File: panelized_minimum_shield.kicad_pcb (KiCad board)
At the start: 2 copper layers, 100 x 78 mm, 91 parts, among them J1 Conn_02x08_Odd_Even, J2 Conn_02x08_Odd_Even, J3 Conn_01x06, SW1 SW_Push

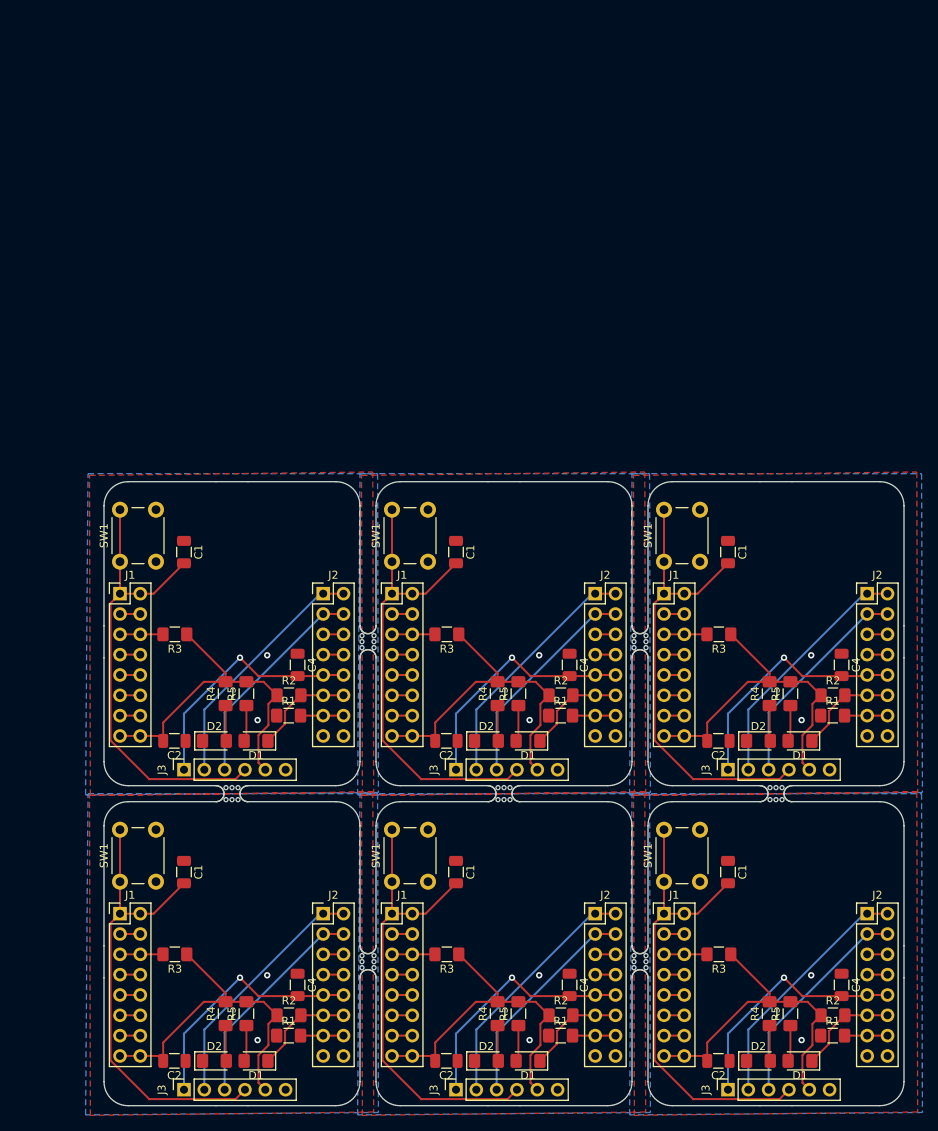
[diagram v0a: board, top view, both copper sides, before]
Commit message: V1.1 - fixing missing ground connection to pull up resistor for GPIO15
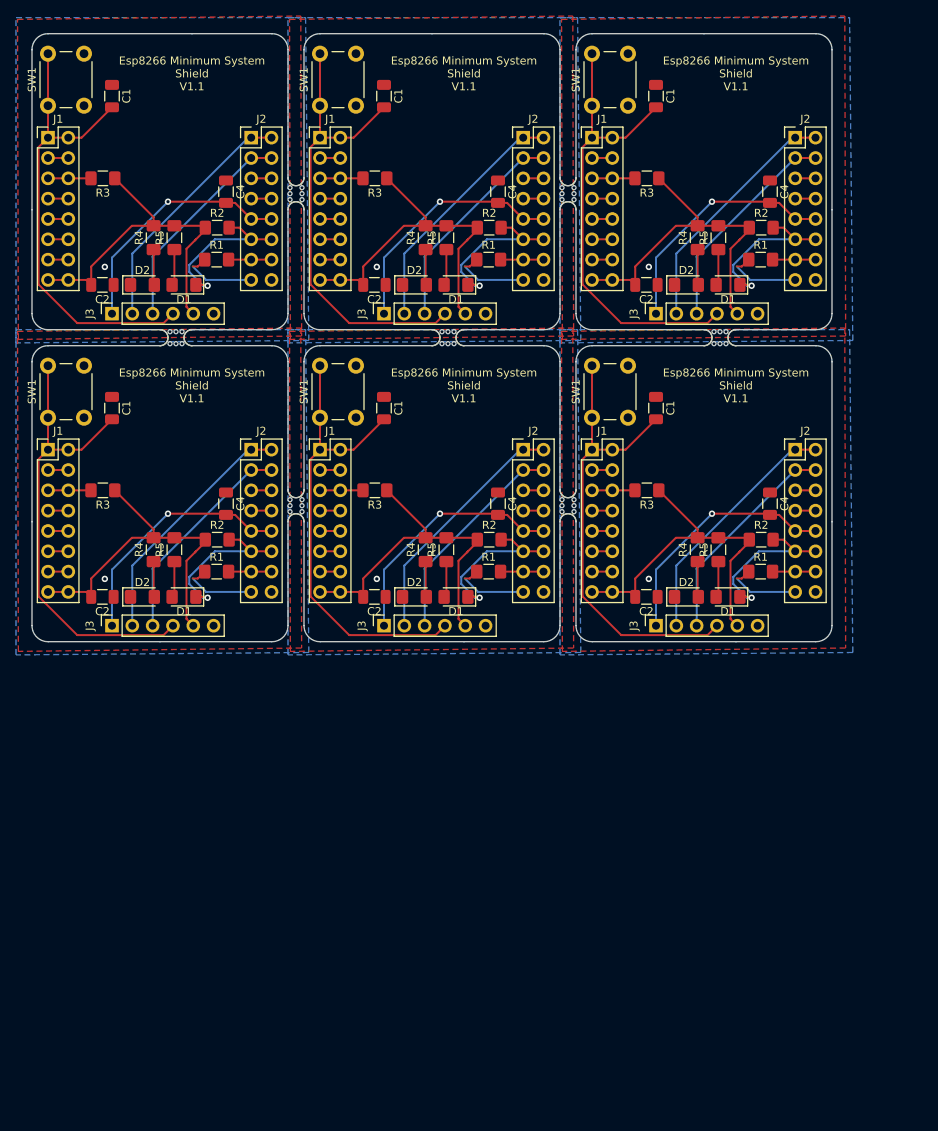
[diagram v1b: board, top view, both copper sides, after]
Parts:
- removed the C1 at (109.0, 128.8)
- removed the C1 at (75.0, 128.8)
- removed the C1 at (41.0, 128.8)
- removed the C1 at (109.0, 88.8)
- removed the C1 at (75.0, 88.8)
- removed the C2 at (107.8, 152.4)
- removed the C2 at (73.8, 152.4)
- removed the C2 at (39.8, 152.4)
- removed the C2 at (107.8, 112.4)
- removed the C2 at (73.8, 112.4)
- removed the C4 at (123.2, 142.9)
- removed the C4 at (89.2, 142.9)
- removed the C4 at (55.2, 142.9)
- removed the C4 at (123.2, 102.9)
- removed the C4 at (89.2, 102.9)
- removed the D1 at (118.0, 152.4)
- removed the D1 at (84.0, 152.4)
- removed the D1 at (50.0, 152.4)
- removed the D1 at (118.0, 112.4)
- removed the D1 at (84.0, 112.4)
- removed the D2 at (112.8, 152.4)
- removed the D2 at (78.8, 152.4)
- removed the D2 at (44.8, 152.4)
- removed the D2 at (112.8, 112.4)
- removed the D2 at (78.8, 112.4)
- removed the J1 at (101.0, 134.0)
- removed the J1 at (67.0, 134.0)
- removed the J1 at (33.0, 134.0)
- removed the J1 at (101.0, 94.0)
- removed the J1 at (67.0, 94.0)
- removed the J2 at (126.4, 134.0)
- removed the J2 at (92.4, 134.0)
- removed the J2 at (58.4, 134.0)
- removed the J2 at (126.4, 94.0)
- removed the J2 at (92.4, 94.0)
- removed the J3 at (109.0, 156.0)
- removed the J3 at (75.0, 156.0)
- removed the J3 at (41.0, 156.0)
- removed the J3 at (109.0, 116.0)
- removed the J3 at (75.0, 116.0)
- removed the R1 at (122.1, 149.2)
- removed the R1 at (88.1, 149.2)
- removed the R1 at (54.1, 149.2)
- removed the R1 at (122.1, 109.2)
- removed the R1 at (88.1, 109.2)
- removed the R2 at (122.1, 146.7)
- removed the R2 at (88.1, 146.7)
- removed the R2 at (54.1, 146.7)
- removed the R2 at (122.1, 106.7)
- removed the R2 at (88.1, 106.7)
- removed the R3 at (107.9, 139.1)
- removed the R3 at (73.9, 139.1)
- removed the R3 at (39.9, 139.1)
- removed the R3 at (107.9, 99.1)
- removed the R3 at (73.9, 99.1)
- removed the R4 at (114.2, 146.5)
- removed the R4 at (80.2, 146.5)
- removed the R4 at (46.2, 146.5)
- removed the R4 at (114.2, 106.5)
- removed the R4 at (80.2, 106.5)
- removed the R5 at (116.8, 146.5)
- removed the R5 at (82.8, 146.5)
- removed the R5 at (48.8, 146.5)
- removed the R5 at (116.8, 106.5)
- removed the R5 at (82.8, 106.5)
- removed the SW1 at (101.0, 130.0)
- removed the SW1 at (67.0, 130.0)
- removed the SW1 at (33.0, 130.0)
- removed the SW1 at (101.0, 90.0)
- removed the SW1 at (67.0, 90.0)
- removed the mouse-bite-2mm-slot at (98.0, 140.0)
- removed the mouse-bite-2mm-slot at (64.0, 140.0)
- removed the mouse-bite-2mm-slot at (98.0, 100.0)
- removed the mouse-bite-2mm-slot at (64.0, 100.0)
- removed the mouse-bite-2mm-slot at (115.0, 119.0)
- removed the mouse-bite-2mm-slot at (81.0, 119.0)
- removed the mouse-bite-2mm-slot at (47.0, 119.0)
- added C1: 100nf, Capacitor_SMD:C_1206_3216Metric, F.Cu at (100.0, 70.8)
- added C1: 100nf, Capacitor_SMD:C_1206_3216Metric, F.Cu at (66.0, 70.8)
- added C1: 100nf, Capacitor_SMD:C_1206_3216Metric, F.Cu at (32.0, 70.8)
- added C1: 100nf, Capacitor_SMD:C_1206_3216Metric, F.Cu at (100.0, 31.8)
- added C1: 100nf, Capacitor_SMD:C_1206_3216Metric, F.Cu at (66.0, 31.8)
- added C2: 100nf, Capacitor_SMD:C_1206_3216Metric, F.Cu at (98.8, 94.4)
- added C2: 100nf, Capacitor_SMD:C_1206_3216Metric, F.Cu at (64.8, 94.4)
- added C2: 100nf, Capacitor_SMD:C_1206_3216Metric, F.Cu at (30.8, 94.4)
- added C2: 100nf, Capacitor_SMD:C_1206_3216Metric, F.Cu at (98.8, 55.4)
- added C2: 100nf, Capacitor_SMD:C_1206_3216Metric, F.Cu at (64.8, 55.4)
- added C4: 100nf, Capacitor_SMD:C_1206_3216Metric, F.Cu at (114.2, 82.8)
- added C4: 100nf, Capacitor_SMD:C_1206_3216Metric, F.Cu at (80.2, 82.8)
- added C4: 100nf, Capacitor_SMD:C_1206_3216Metric, F.Cu at (46.2, 82.8)
- added C4: 100nf, Capacitor_SMD:C_1206_3216Metric, F.Cu at (114.2, 43.8)
- added C4: 100nf, Capacitor_SMD:C_1206_3216Metric, F.Cu at (80.2, 43.8)
- added D1: GREEN, LED_SMD:LED_1206_3216Metric_Pad1.42x1.75mm_HandSolder, F.Cu at (109.0, 94.4)
- added D1: GREEN, LED_SMD:LED_1206_3216Metric_Pad1.42x1.75mm_HandSolder, F.Cu at (75.0, 94.4)
- added D1: GREEN, LED_SMD:LED_1206_3216Metric_Pad1.42x1.75mm_HandSolder, F.Cu at (41.0, 94.4)
- added D1: GREEN, LED_SMD:LED_1206_3216Metric_Pad1.42x1.75mm_HandSolder, F.Cu at (109.0, 55.4)
- added D1: GREEN, LED_SMD:LED_1206_3216Metric_Pad1.42x1.75mm_HandSolder, F.Cu at (75.0, 55.4)
- added D2: RED, LED_SMD:LED_1206_3216Metric_Pad1.42x1.75mm_HandSolder, F.Cu at (103.8, 94.4)
- added D2: RED, LED_SMD:LED_1206_3216Metric_Pad1.42x1.75mm_HandSolder, F.Cu at (69.8, 94.4)
- added D2: RED, LED_SMD:LED_1206_3216Metric_Pad1.42x1.75mm_HandSolder, F.Cu at (35.8, 94.4)
- added D2: RED, LED_SMD:LED_1206_3216Metric_Pad1.42x1.75mm_HandSolder, F.Cu at (103.8, 55.4)
- added D2: RED, LED_SMD:LED_1206_3216Metric_Pad1.42x1.75mm_HandSolder, F.Cu at (69.8, 55.4)
- added J1: Conn_02x08_Odd_Even, Connector_PinHeader_2.54mm:PinHeader_2x08_P2.54mm_Vertical, F.Cu at (92.0, 76.0)
- added J1: Conn_02x08_Odd_Even, Connector_PinHeader_2.54mm:PinHeader_2x08_P2.54mm_Vertical, F.Cu at (58.0, 76.0)
- added J1: Conn_02x08_Odd_Even, Connector_PinHeader_2.54mm:PinHeader_2x08_P2.54mm_Vertical, F.Cu at (24.0, 76.0)
- added J1: Conn_02x08_Odd_Even, Connector_PinHeader_2.54mm:PinHeader_2x08_P2.54mm_Vertical, F.Cu at (92.0, 37.0)
- added J1: Conn_02x08_Odd_Even, Connector_PinHeader_2.54mm:PinHeader_2x08_P2.54mm_Vertical, F.Cu at (58.0, 37.0)
- added J2: Conn_02x08_Odd_Even, Connector_PinHeader_2.54mm:PinHeader_2x08_P2.54mm_Vertical, F.Cu at (117.4, 76.0)
- added J2: Conn_02x08_Odd_Even, Connector_PinHeader_2.54mm:PinHeader_2x08_P2.54mm_Vertical, F.Cu at (83.4, 76.0)
- added J2: Conn_02x08_Odd_Even, Connector_PinHeader_2.54mm:PinHeader_2x08_P2.54mm_Vertical, F.Cu at (49.4, 76.0)
- added J2: Conn_02x08_Odd_Even, Connector_PinHeader_2.54mm:PinHeader_2x08_P2.54mm_Vertical, F.Cu at (117.4, 37.0)
- added J2: Conn_02x08_Odd_Even, Connector_PinHeader_2.54mm:PinHeader_2x08_P2.54mm_Vertical, F.Cu at (83.4, 37.0)
- added J3: Conn_01x06, Connector_PinSocket_2.54mm:PinSocket_1x06_P2.54mm_Vertical, F.Cu at (100.0, 98.0)
- added J3: Conn_01x06, Connector_PinSocket_2.54mm:PinSocket_1x06_P2.54mm_Vertical, F.Cu at (66.0, 98.0)
- added J3: Conn_01x06, Connector_PinSocket_2.54mm:PinSocket_1x06_P2.54mm_Vertical, F.Cu at (32.0, 98.0)
- added J3: Conn_01x06, Connector_PinSocket_2.54mm:PinSocket_1x06_P2.54mm_Vertical, F.Cu at (100.0, 59.0)
- added J3: Conn_01x06, Connector_PinSocket_2.54mm:PinSocket_1x06_P2.54mm_Vertical, F.Cu at (66.0, 59.0)
- added R1: 10k, Resistor_SMD:R_1206_3216Metric_Pad1.42x1.75mm_HandSolder, F.Cu at (113.1, 91.2)
- added R1: 10k, Resistor_SMD:R_1206_3216Metric_Pad1.42x1.75mm_HandSolder, F.Cu at (79.1, 91.2)
- added R1: 10k, Resistor_SMD:R_1206_3216Metric_Pad1.42x1.75mm_HandSolder, F.Cu at (45.1, 91.2)
- added R1: 10k, Resistor_SMD:R_1206_3216Metric_Pad1.42x1.75mm_HandSolder, F.Cu at (113.1, 52.2)
- added R1: 10k, Resistor_SMD:R_1206_3216Metric_Pad1.42x1.75mm_HandSolder, F.Cu at (79.1, 52.2)
- added R2: 5k1, Resistor_SMD:R_1206_3216Metric_Pad1.42x1.75mm_HandSolder, F.Cu at (113.2, 87.2)
- added R2: 5k1, Resistor_SMD:R_1206_3216Metric_Pad1.42x1.75mm_HandSolder, F.Cu at (79.2, 87.2)
- added R2: 5k1, Resistor_SMD:R_1206_3216Metric_Pad1.42x1.75mm_HandSolder, F.Cu at (45.1, 87.2)
- added R2: 5k1, Resistor_SMD:R_1206_3216Metric_Pad1.42x1.75mm_HandSolder, F.Cu at (113.2, 48.2)
- added R2: 5k1, Resistor_SMD:R_1206_3216Metric_Pad1.42x1.75mm_HandSolder, F.Cu at (79.2, 48.2)
- added R3: 5k1, Resistor_SMD:R_1206_3216Metric_Pad1.42x1.75mm_HandSolder, F.Cu at (98.9, 81.1)
- added R3: 5k1, Resistor_SMD:R_1206_3216Metric_Pad1.42x1.75mm_HandSolder, F.Cu at (64.9, 81.1)
- added R3: 5k1, Resistor_SMD:R_1206_3216Metric_Pad1.42x1.75mm_HandSolder, F.Cu at (30.9, 81.1)
- added R3: 5k1, Resistor_SMD:R_1206_3216Metric_Pad1.42x1.75mm_HandSolder, F.Cu at (98.9, 42.1)
- added R3: 5k1, Resistor_SMD:R_1206_3216Metric_Pad1.42x1.75mm_HandSolder, F.Cu at (64.9, 42.1)
- added R4: 220, Resistor_SMD:R_1206_3216Metric_Pad1.42x1.75mm_HandSolder, F.Cu at (105.2, 88.5)
- added R4: 220, Resistor_SMD:R_1206_3216Metric_Pad1.42x1.75mm_HandSolder, F.Cu at (71.2, 88.5)
- added R4: 220, Resistor_SMD:R_1206_3216Metric_Pad1.42x1.75mm_HandSolder, F.Cu at (37.2, 88.5)
- added R4: 220, Resistor_SMD:R_1206_3216Metric_Pad1.42x1.75mm_HandSolder, F.Cu at (105.2, 49.5)
- added R4: 220, Resistor_SMD:R_1206_3216Metric_Pad1.42x1.75mm_HandSolder, F.Cu at (71.2, 49.5)
- added R5: 220, Resistor_SMD:R_1206_3216Metric_Pad1.42x1.75mm_HandSolder, F.Cu at (107.8, 88.5)
- added R5: 220, Resistor_SMD:R_1206_3216Metric_Pad1.42x1.75mm_HandSolder, F.Cu at (73.8, 88.5)
- added R5: 220, Resistor_SMD:R_1206_3216Metric_Pad1.42x1.75mm_HandSolder, F.Cu at (39.8, 88.5)
- added R5: 220, Resistor_SMD:R_1206_3216Metric_Pad1.42x1.75mm_HandSolder, F.Cu at (107.8, 49.5)
- added R5: 220, Resistor_SMD:R_1206_3216Metric_Pad1.42x1.75mm_HandSolder, F.Cu at (73.8, 49.5)
- added SW1: SW_Push, Button_Switch_THT:SW_PUSH_6mm, F.Cu at (92.0, 72.0)
- added SW1: SW_Push, Button_Switch_THT:SW_PUSH_6mm, F.Cu at (58.0, 72.0)
- added SW1: SW_Push, Button_Switch_THT:SW_PUSH_6mm, F.Cu at (24.0, 72.0)
- added SW1: SW_Push, Button_Switch_THT:SW_PUSH_6mm, F.Cu at (92.0, 33.0)
- added SW1: SW_Push, Button_Switch_THT:SW_PUSH_6mm, F.Cu at (58.0, 33.0)
- added mouse-bite-2mm-slot: VAL**, Panelization:mouse-bite-2mm-slot, F.Cu at (89.0, 83.0)
- added mouse-bite-2mm-slot: VAL**, Panelization:mouse-bite-2mm-slot, F.Cu at (55.0, 83.0)
- added mouse-bite-2mm-slot: VAL**, Panelization:mouse-bite-2mm-slot, F.Cu at (89.0, 44.0)
- added mouse-bite-2mm-slot: VAL**, Panelization:mouse-bite-2mm-slot, F.Cu at (55.0, 44.0)
- added mouse-bite-2mm-slot: VAL**, Panelization:mouse-bite-2mm-slot, F.Cu at (108.0, 62.0)
- added mouse-bite-2mm-slot: VAL**, Panelization:mouse-bite-2mm-slot, F.Cu at (74.0, 62.0)
- added mouse-bite-2mm-slot: VAL**, Panelization:mouse-bite-2mm-slot, F.Cu at (40.0, 62.0)
- moved C4 59.8 mm to (46.2, 43.8)
- moved R2 59.1 mm to (45.1, 48.2)
- moved C2 57.7 mm to (30.8, 55.4)
- moved D1 57.7 mm to (41.0, 55.4)
- moved D2 57.7 mm to (35.8, 55.4)
- moved C1 57.7 mm to (32.0, 31.8)
- moved J1 57.7 mm to (24.0, 37.0)
- moved J2 57.7 mm to (49.4, 37.0)
- moved J3 57.7 mm to (32.0, 59.0)
- moved R3 57.7 mm to (30.9, 42.1)
- moved R4 57.7 mm to (37.2, 49.5)
- moved R5 57.7 mm to (39.8, 49.5)
- moved SW1 57.7 mm to (24.0, 33.0)
- moved R1 57.7 mm to (45.1, 52.2)
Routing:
- net GND: track 0.00 -> 59.1 mm, vias 12 -> 6
- net IO2: track 76.4 -> 122.2 mm, vias 0 -> 6
- net VCC: track 263.8 -> 270.2 mm
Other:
- board size 100 x 78 mm -> 100 x 76 mm
- board text added: "Esp8266 Minimum System Shield V1.1"
- board text removed: "GPIO2"
